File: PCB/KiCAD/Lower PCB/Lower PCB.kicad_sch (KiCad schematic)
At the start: 118 parts, among them IC1 ADG608BRZ, IC2 ADG608BRZ, IC3 ADG608BRZ, J1 Conn_01x02_MountingPin, J2 Conn_01x04_MountingPin, J3 Conn_01x04_MountingPin, J4 Conn_01x04_MountingPin, Q1 SFH320, Q10 SFH320, Q11 SFH320, Q12 SFH320, Q13 SFH320, Q14 SFH320, Q15 SFH320, Q16 SFH320, Q17 SFH320, Q18 SFH320, Q19 SFH320, Q2 SFH320, Q20 SFH320, Q21 SFH320, Q22 SFH320, Q23 SFH320, Q24 SFH320, Q3 SFH320, Q4 SFH320, Q5 SFH320, Q6 SFH320, Q7 SFH320, Q8 SFH320, Q9 SFH320

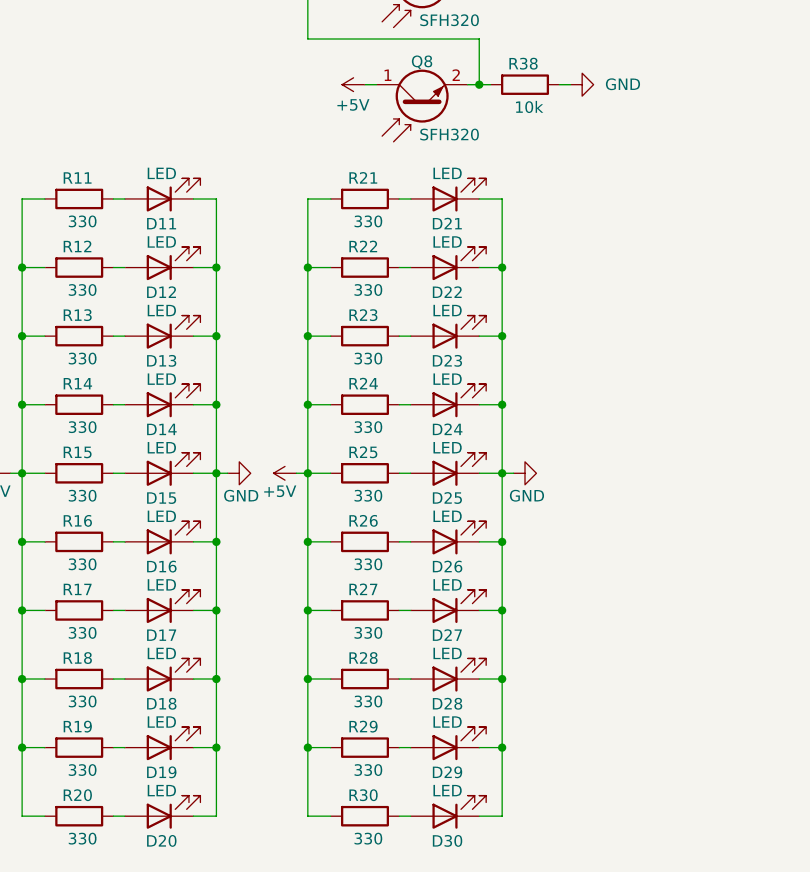
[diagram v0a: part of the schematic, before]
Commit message: Positioned LDRs and LEDs
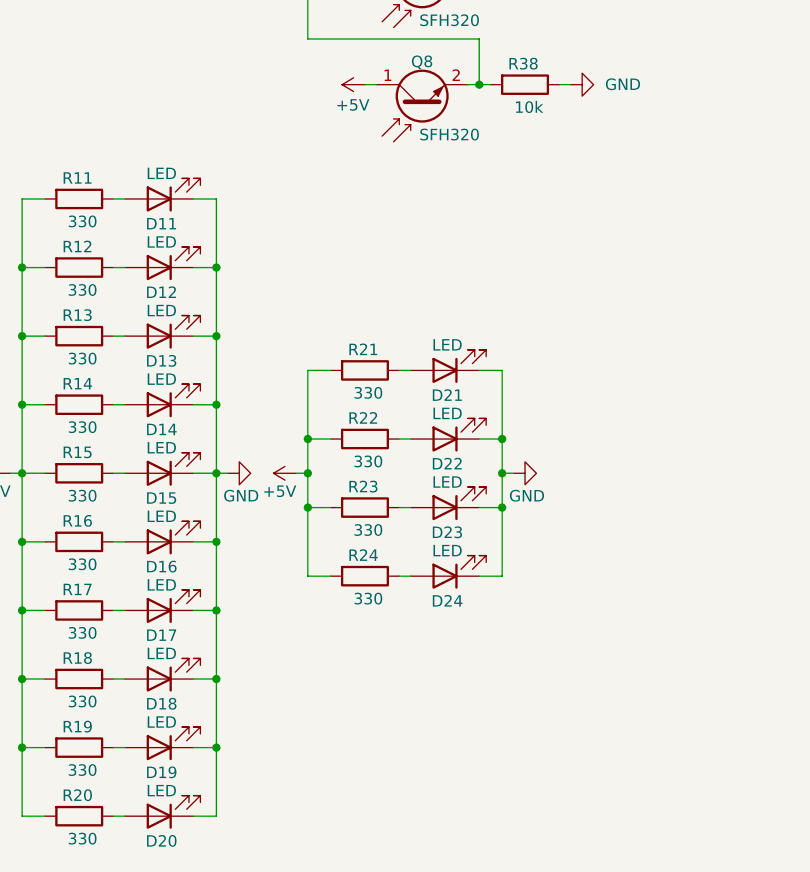
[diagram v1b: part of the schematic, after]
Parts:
- removed D25, D26, D27, D28, D29, D30: LED, LED_SMD:LED_PLCC-2_3.4x3.0mm_KA, symbol Device:LED
- removed R25, R26, R27, R28, R29, R30: 330, Resistor_SMD:R_0805_2012Metric_Pad1.20x1.40mm_HandSolder, symbol Device:R
- J3, J4: footprint Connector_JST:JST_PH_B4B-PH-SM4-TB_1x04-1MP_P2.00mm_Vertical -> Connector_JST:JST_PH_S4B-PH-SM4-TB_1x04-1MP_P2.00mm_Horizontal
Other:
- moved on the sheet: D21, D22, D23, D24, R21, R22, R23, R24

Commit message: Cleaned up LDR and LED locations
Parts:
- J1: footprint Connector_JST:JST_PH_B2B-PH-SM4-TB_1x02-1MP_P2.00mm_Vertical -> Connector_JST:JST_PH_S2B-PH-SM4-TB_1x02-1MP_P2.00mm_Horizontal
- J2: footprint Connector_JST:JST_PH_B4B-PH-SM4-TB_1x04-1MP_P2.00mm_Vertical -> Connector_JST:JST_PH_S4B-PH-SM4-TB_1x04-1MP_P2.00mm_Horizontal
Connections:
- net +3V3: now also C1.1, C2.1, C3.1, IC1.13 (VDD), IC1.2 (EN), IC2.13 (VDD), IC2.2 (EN), IC3.13 (VDD), IC3.2 (EN), R1.2, R10.2, R11.2, R12.2, R13.2, R14.2, R15.2, R16.2, R17.2, R18.2, R19.2, R2.2, R20.2, R21.2, R22.2, R23.2, R24.2, R3.2, R4.2, R5.2, R6.2, R7.2, R8.2, R9.2
- net +5V: no longer C1.1, C2.1, C3.1, IC1.13 (VDD), IC1.2 (EN), IC2.13 (VDD), IC2.2 (EN), IC3.13 (VDD), IC3.2 (EN), R1.2, R10.2, R11.2, R12.2, R13.2, R14.2, R15.2, R16.2, R17.2, R18.2, R19.2, R2.2, R20.2, R21.2, R22.2, R23.2, R24.2, R3.2, R4.2, R5.2, R6.2, R7.2, R8.2, R9.2

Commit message: Uh oh there was a +5V rail
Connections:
- net +5V is gone; now on net +3V3: Q1.1 (C), Q10.1 (C), Q11.1 (C), Q12.1 (C), Q13.1 (C), Q14.1 (C), Q15.1 (C), Q16.1 (C), Q17.1 (C), Q18.1 (C), Q19.1 (C), Q2.1 (C), Q20.1 (C), Q21.1 (C), Q22.1 (C), Q23.1 (C), Q24.1 (C), Q3.1 (C), Q4.1 (C), Q5.1 (C), Q6.1 (C), Q7.1 (C), Q8.1 (C), Q9.1 (C)
